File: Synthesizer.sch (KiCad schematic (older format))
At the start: 39 parts, among them J9 MCU_debug, SW1 SW_Push, SW10 SW_Push, SW11 SW_Push, SW12 SW_Push, SW13 SW_Push, SW2 SW_Push, SW3 SW_Push, SW4 SW_Push, SW5 SW_Push, SW6 SW_Push, SW7 SW_Push, SW8 SW_Push, SW9 SW_Push, U1 EFM32GG11B1xx, U7 EFM32GG11B1xx, Y1 48Mhz

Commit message: Added audio jack and footprint
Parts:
- added J2: AudioJack3, Connector_Audio:Jack_3.5mm_CUI_SJ-3524-SMT_Horizontal, symbol Connector:AudioJack3
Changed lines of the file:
@@
 	5350 15650 5350 15350
 Connection ~ 5350 15350
-	14050 4200 14050 4900
 Wire Wire Line
 	10250 5300 10700 5300
@@
 Wire Wire Line
 	8500 9050 9150 9050
+$Comp
+L Connector:AudioJack3 J2
+U 1 1 5D83EB38
+P 2500 10100
+F 0 "J2" H 2482 10425 50  0000 C CNN
+F 1 "AudioJack3" H 2482 10334 50  0000 C CNN
+F 2 "Connector_Audio:Jack_3.5mm_CUI_SJ-3524-SMT_Horizontal" H 2500 10100 50  0001 C CNN
+F 3 "~" H 2500 10100 50  0001 C CNN
+	1    2500 10100
+	1    0    0    -1
+$EndComp
 $EndSCHEMATC

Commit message: Change the project to use the new MCU
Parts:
- removed C1: 1u, Capacitor_SMD:C_0805_2012Metric_Pad1.15x1.40mm_HandSolder, symbol Device:C
- removed C2, C3, C5, C6, C7, C8: 100n, Capacitor_SMD:C_0805_2012Metric_Pad1.15x1.40mm_HandSolder, symbol Device:C
- removed C4, C9: 10u, Capacitor_SMD:C_0805_2012Metric_Pad1.15x1.40mm_HandSolder, symbol Device:CP1
- removed J9: MCU_debug, Connector_PinHeader_2.54mm:PinHeader_2x10_P2.54mm_Vertical, symbol Synth:MCU_debug
- removed U1: EFM32GG11B1xx, Package_QFP:HTQFP-64-1EP_10x10mm_P0.5mm_EP8x8mm, symbol Synth:EFM32GG11B1xx
- removed U7: EFM32GG11B1xx, Package_QFP:TQFP-64_10x10mm_P0.5mm, symbol Synth:EFM32GG11B1xx
- removed Y1: 48Mhz, Crystal:Crystal_DS10_D1.0mm_L4.3mm_Vertical, symbol Device:Crystal
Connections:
- wire segments 125 -> 63
- no-connect marks 35 -> 1
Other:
- note removed: "10 times samplerate?"
- note removed: "decouplers for the MCU"

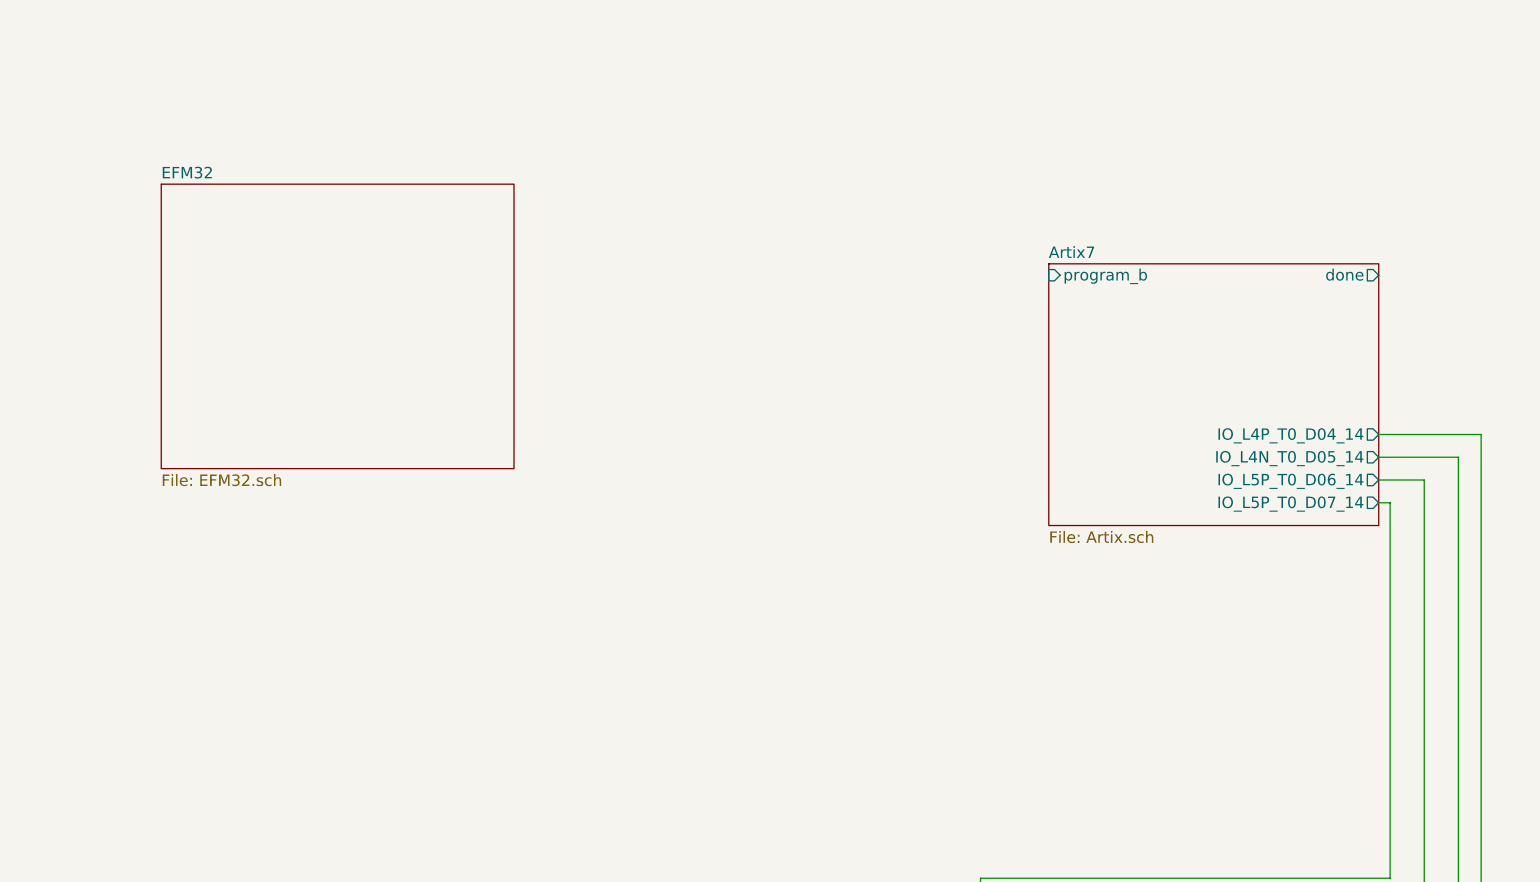
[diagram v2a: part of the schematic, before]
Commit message: Connect the MCU SPI pins to FPGA
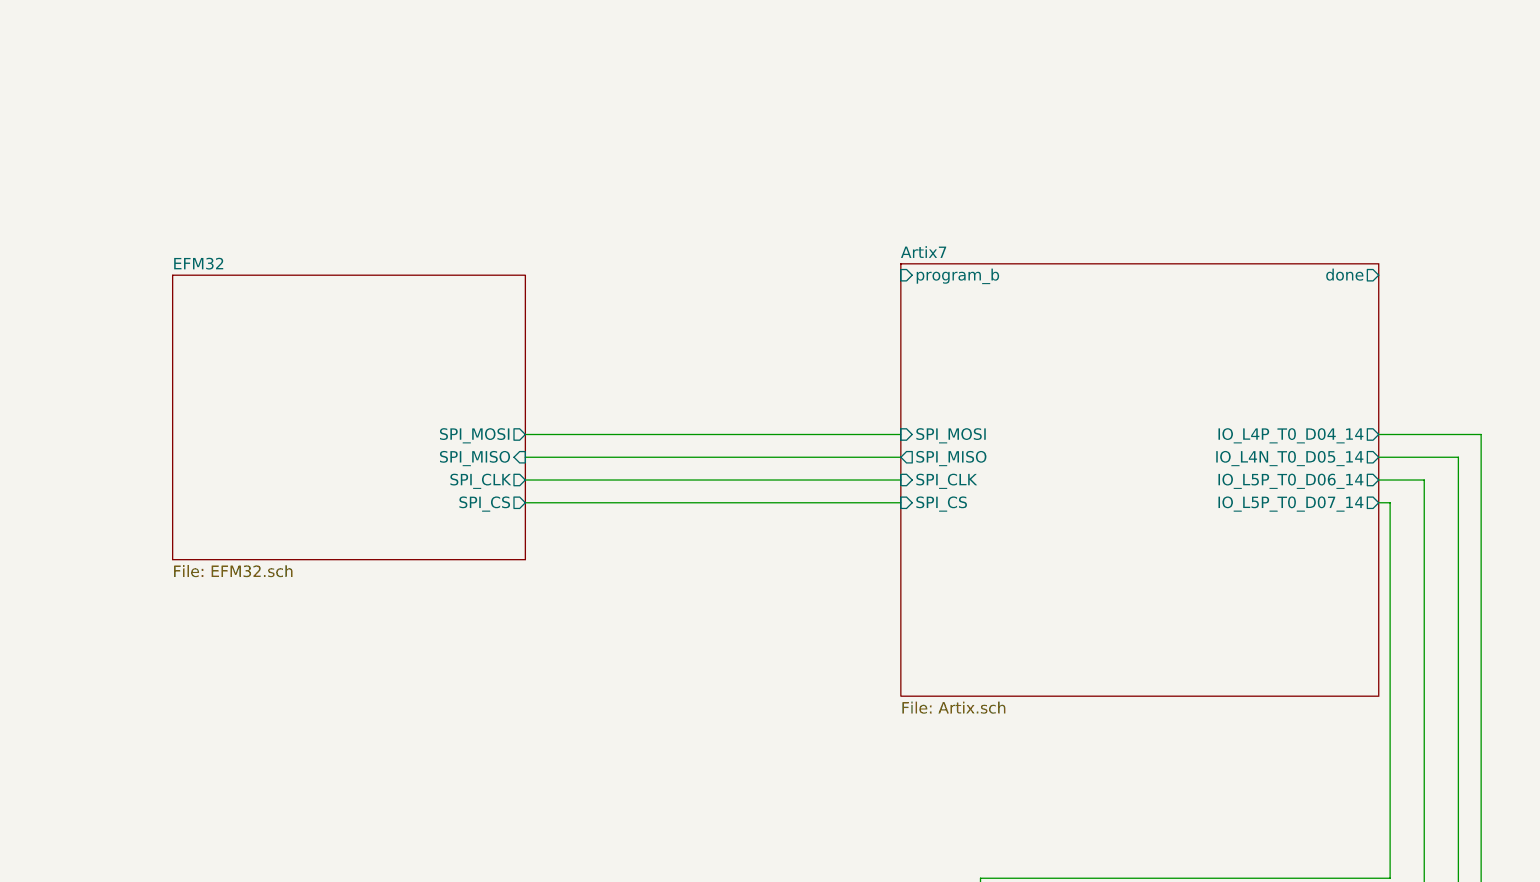
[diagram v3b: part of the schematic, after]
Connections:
- wire segments 63 -> 67
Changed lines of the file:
@@
 $EndDescr
 $Sheet
-S 8800 4550 1450 1150
+S 8150 4550 2100 1900
 U 5D81B1F5
 F0 "Artix7" 50
 F1 "Artix.sch" 50
-F2 "program_b" I L 8800 4600 50
+F2 "program_b" I L 8150 4600 50
 F3 "IO_L4P_T0_D04_14" O R 10250 5300 50
 F4 "IO_L4N_T0_D05_14" O R 10250 5400 50
@@
 F6 "IO_L5P_T0_D07_14" O R 10250 5600 50
 F7 "done" O R 10250 4600 50
+F8 "SPI_MOSI" I L 8150 5300 50
+F9 "SPI_MISO" O L 8150 5400 50
+F10 "SPI_CLK" I L 8150 5500 50
+F11 "SPI_CS" I L 8150 5600 50
 $EndSheet
 $Sheet
@@
 $EndComp
 $Sheet
-S 4900 4200 1550 1250
+S 4950 4600 1550 1250
 U 5D8502F2
 F0 "EFM32" 50
 F1 "EFM32.sch" 50
+F2 "SPI_MISO" I R 6500 5400 50
+F3 "SPI_CLK" O R 6500 5500 50
+F4 "SPI_CS" O R 6500 5600 50
+F5 "SPI_MOSI" O R 6500 5300 50
 $EndSheet
+Wire Wire Line
+	6500 5300 8150 5300
+Wire Wire Line
+	6500 5400 8150 5400
+Wire Wire Line
+	6500 5500 8150 5500
+Wire Wire Line
+	8150 5600 6500 5600
 $EndSCHEMATC

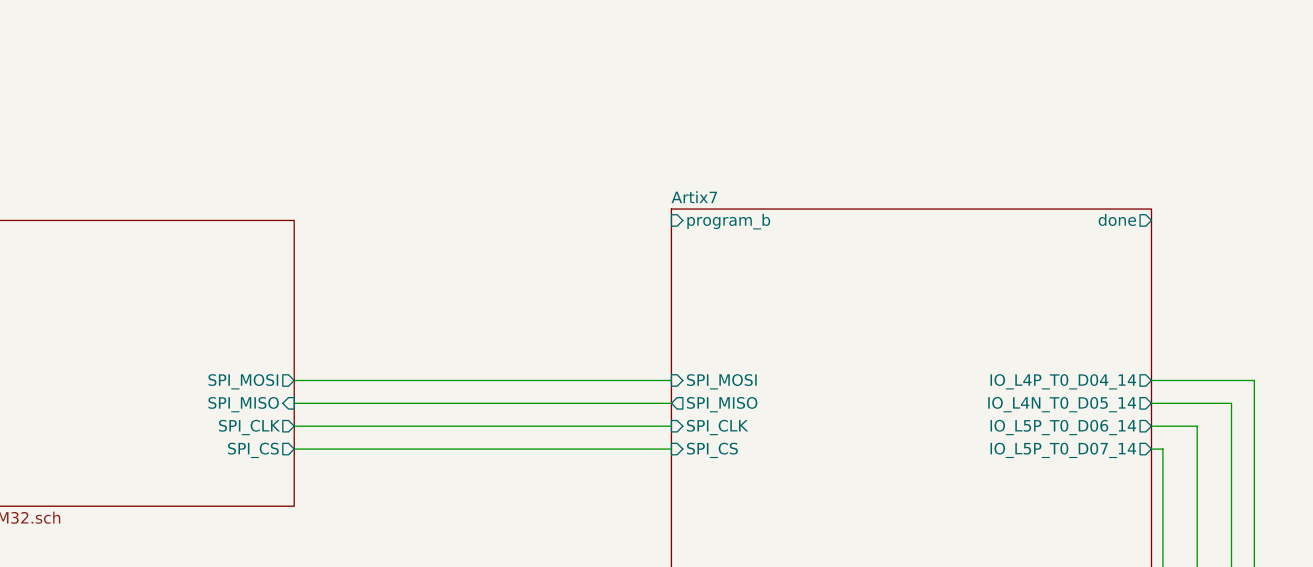
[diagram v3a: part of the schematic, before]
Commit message: Connect FPGA done and program_b pin to some pins on the MCU
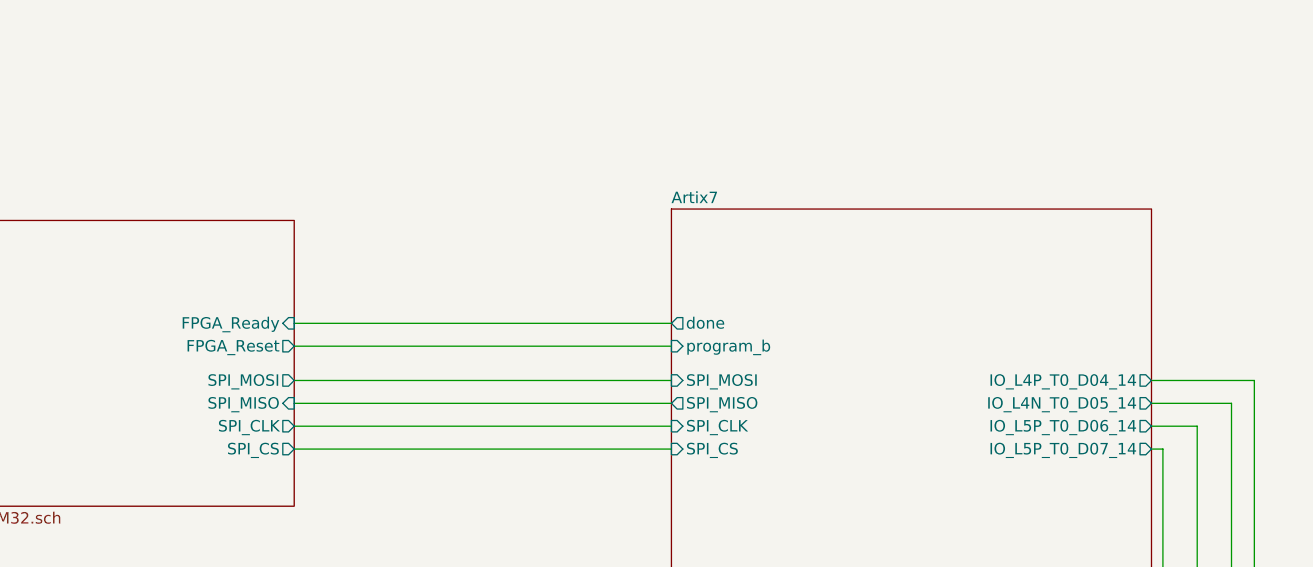
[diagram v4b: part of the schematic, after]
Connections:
- wire segments 67 -> 69
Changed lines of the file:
@@
 EESchema Schematic File Version 4
+LIBS:Synthesizer-cache
 EELAYER 30 0
 EELAYER END
@@
 F0 "Artix7" 50
 F1 "Artix.sch" 50
-F2 "program_b" I L 8150 4600 50
+F2 "program_b" I L 8150 5150 50
 F3 "IO_L4P_T0_D04_14" O R 10250 5300 50
 F4 "IO_L4N_T0_D05_14" O R 10250 5400 50
 F5 "IO_L5P_T0_D06_14" O R 10250 5500 50
 F6 "IO_L5P_T0_D07_14" O R 10250 5600 50
-F7 "done" O R 10250 4600 50
+F7 "done" O L 8150 5050 50
 F8 "SPI_MOSI" I L 8150 5300 50
 F9 "SPI_MISO" O L 8150 5400 50
@@
 F4 "SPI_CS" O R 6500 5600 50
 F5 "SPI_MOSI" O R 6500 5300 50
+F6 "FPGA_Ready" I R 6500 5050 50
+F7 "FPGA_Reset" O R 6500 5150 50
 $EndSheet
 Wire Wire Line
@@
 Wire Wire Line
 	8150 5600 6500 5600
+Wire Wire Line
+	6500 5150 8150 5150
+Wire Wire Line
+	8150 5050 6500 5050
 $EndSCHEMATC

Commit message: Add USB symbol and pins
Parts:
- added J?: USB_B, symbol Connector:USB_B
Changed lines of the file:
@@
 Wire Wire Line
 	8150 5050 6500 5050
+$Comp
+L Connector:USB_B J?
+U 1 1 5D8E7346
+P 1600 5100
+F 0 "J?" H 1657 5567 50  0000 C CNN
+F 1 "USB_B" H 1657 5476 50  0000 C CNN
+F 2 "" H 1750 5050 50  0001 C CNN
+F 3 " ~" H 1750 5050 50  0001 C CNN
+	1    1600 5100
+	1    0    0    -1
+$EndComp
 $EndSCHEMATC

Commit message: Wired up minijack and micro-USB.
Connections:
- wire segments 69 -> 74
- no-connect marks 1 -> 4
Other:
- note added: "I think this makes sense?"
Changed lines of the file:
@@
 EESchema Schematic File Version 4
-LIBS:Synthesizer-cache
 EELAYER 30 0
 EELAYER END
@@
 $EndSheet
 $Sheet
-S 13750 7050 2150 1400
+S 15050 4300 2150 1400
 U 5DC1AA2E
 F0 "PSU" 50
 F1 "PSU.sch" 50
-F2 "POWER_IN" I L 13750 7200 50
-F3 "3.3V" I R 15900 7350 50
-F4 "3.3VA" I R 15900 7450 50
-F5 "1.8V" I R 15900 7250 50
-F6 "1.0V" I R 15900 7150 50
+F2 "POWER_IN" I L 15050 4450 50
+F3 "3.3V" I R 17200 4600 50
+F4 "3.3VA" I R 17200 4700 50
+F5 "1.8V" I R 17200 4500 50
+F6 "1.0V" I R 17200 4400 50
 $EndSheet
-$Comp
-L power:VCC #PWR0101
-U 1 1 5DF2B372
-P 13450 7200
-F 0 "#PWR0101" H 13450 7050 50  0001 C CNN
-F 1 "VCC" V 13468 7327 50  0000 L CNN
-F 2 "" H 13450 7200 50  0001 C CNN
-F 3 "" H 13450 7200 50  0001 C CNN
-	1    13450 7200
-	0    -1   -1   0
-$EndComp
-Wire Wire Line
-	13450 7200 13750 7200
-Wire Wire Line
-	15900 7250 16100 7250
-Wire Wire Line
-	16100 7350 15900 7350
-Wire Wire Line
-	15900 7450 16100 7450
+Wire Wire Line
+	17200 4500 17400 4500
+Wire Wire Line
+	17400 4600 17200 4600
+Wire Wire Line
+	17200 4700 17400 4700
 Wire Wire Line
 	5300 2200 5300 2400
@@
 L power:+1V8 #PWR0106
 U 1 1 5E05CCC0
-P 16100 7250
-F 0 "#PWR0106" H 16100 7100 50  0001 C CNN
-F 1 "+1V8" V 16115 7378 50  0000 L CNN
-F 2 "" H 16100 7250 50  0001 C CNN
-F 3 "" H 16100 7250 50  0001 C CNN
-	1    16100 7250
+P 17400 4500
+F 0 "#PWR0106" H 17400 4350 50  0001 C CNN
+F 1 "+1V8" V 17415 4628 50  0000 L CNN
+F 2 "" H 17400 4500 50  0001 C CNN
+F 3 "" H 17400 4500 50  0001 C CNN
+	1    17400 4500
 	0    1    1    0
 $EndComp
@@
 L power:+3.3V #PWR0107
 U 1 1 5E05D9B9
-P 16100 7350
-F 0 "#PWR0107" H 16100 7200 50  0001 C CNN
-F 1 "+3.3V" V 16115 7478 50  0000 L CNN
-F 2 "" H 16100 7350 50  0001 C CNN
-F 3 "" H 16100 7350 50  0001 C CNN
-	1    16100 7350
+P 17400 4600
+F 0 "#PWR0107" H 17400 4450 50  0001 C CNN
+F 1 "+3.3V" V 17415 4728 50  0000 L CNN
+F 2 "" H 17400 4600 50  0001 C CNN
+F 3 "" H 17400 4600 50  0001 C CNN
+	1    17400 4600
 	0    1    1    0
 $EndComp
@@
 L power:+3.3VA #PWR0108
 U 1 1 5E05DF67
-P 16100 7450
-F 0 "#PWR0108" H 16100 7300 50  0001 C CNN
-F 1 "+3.3VA" V 16115 7578 50  0000 L CNN
-F 2 "" H 16100 7450 50  0001 C CNN
-F 3 "" H 16100 7450 50  0001 C CNN
-	1    16100 7450
+P 17400 4700
+F 0 "#PWR0108" H 17400 4550 50  0001 C CNN
+F 1 "+3.3VA" V 17415 4828 50  0000 L CNN
+F 2 "" H 17400 4700 50  0001 C CNN
+F 3 "" H 17400 4700 50  0001 C CNN
+	1    17400 4700
 	0    1    1    0
 $EndComp
@@
 	4900 2200 4900 2400
 Wire Wire Line
-	16100 7150 15900 7150
+	17400 4400 17200 4400
 $Comp
 L power:+1V0 #PWR0105
 U 1 1 5E05BC61
-P 16100 7150
-F 0 "#PWR0105" H 16100 7000 50  0001 C CNN
-F 1 "+1V0" V 16115 7278 50  0000 L CNN
-F 2 "" H 16100 7150 50  0001 C CNN
-F 3 "" H 16100 7150 50  0001 C CNN
-	1    16100 7150
+P 17400 4400
+F 0 "#PWR0105" H 17400 4250 50  0001 C CNN
+F 1 "+1V0" V 17415 4528 50  0000 L CNN
+F 2 "" H 17400 4400 50  0001 C CNN
+F 3 "" H 17400 4400 50  0001 C CNN
+	1    17400 4400
 	0    1    1    0
 $EndComp
@@
 L Connector:AudioJack3 J2
 U 1 1 5D83EB38
-P 2500 10100
-F 0 "J2" H 2482 10425 50  0000 C CNN
-F 1 "AudioJack3" H 2482 10334 50  0000 C CNN
-F 2 "Connector_Audio:Jack_3.5mm_CUI_SJ-3524-SMT_Horizontal" H 2500 10100 50  0001 C CNN
-F 3 "~" H 2500 10100 50  0001 C CNN
-	1    2500 10100
-	1    0    0    -1
+P 12200 8200
+F 0 "J2" H 12182 8525 50  0000 C CNN
+F 1 "AudioJack3" H 12182 8434 50  0000 C CNN
+F 2 "Connector_Audio:Jack_3.5mm_CUI_SJ-3524-SMT_Horizontal" H 12200 8200 50  0001 C CNN
+F 3 "~" H 12200 8200 50  0001 C CNN
+	1    12200 8200
+	-1   0    0    1
 $EndComp
 $Sheet
@@
 L Connector:USB_B J?
 U 1 1 5D8E7346
-P 1600 5100
-F 0 "J?" H 1657 5567 50  0000 C CNN
-F 1 "USB_B" H 1657 5476 50  0000 C CNN
-F 2 "" H 1750 5050 50  0001 C CNN
-F 3 " ~" H 1750 5050 50  0001 C CNN
-	1    1600 5100
-	1    0    0    -1
-$EndComp
+P 14350 4650
+F 0 "J?" H 14407 5117 50  0000 C CNN
+F 1 "USB_B" H 14407 5026 50  0000 C CNN
+F 2 "" H 14500 4600 50  0001 C CNN
+F 3 " ~" H 14500 4600 50  0001 C CNN
+	1    14350 4650
+	1    0    0    -1
+$EndComp
+Wire Wire Line
+	11750 8200 12000 8200
+Wire Wire Line
+	11750 8100 12000 8100
+$Comp
+L power:GND #PWR?
+U 1 1 5D88FD38
+P 11900 8400
+F 0 "#PWR?" H 11900 8150 50  0001 C CNN
+F 1 "GND" H 11905 8227 50  0000 C CNN
+F 2 "" H 11900 8400 50  0001 C CNN
+F 3 "" H 11900 8400 50  0001 C CNN
+	1    11900 8400
+	1    0    0    -1
+$EndComp
+Wire Wire Line
+	12000 8300 11900 8300
+Wire Wire Line
+	11900 8300 11900 8400
+$Comp
+L power:GND #PWR?
+U 1 1 5D894417
+P 14350 5200
+F 0 "#PWR?" H 14350 4950 50  0001 C CNN
+F 1 "GND" H 14355 5027 50  0000 C CNN
+F 2 "" H 14350 5200 50  0001 C CNN
+F 3 "" H 14350 5200 50  0001 C CNN
+	1    14350 5200
+	1    0    0    -1
+$EndComp
+Wire Wire Line
+	14350 5050 14350 5200
+Wire Wire Line
+	14650 4450 15050 4450
+NoConn ~ 14650 4650
+NoConn ~ 14650 4750
+NoConn ~ 14250 5050
+Text Notes 14000 4100 0    50   ~ 0
+I think this makes sense?
 $EndSCHEMATC

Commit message: Wired USB-A. Added a capacitor to USB_VBUS in the schematic. No idea what to do about VBUSEN though.
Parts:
- added J?: USB_A, symbol Connector:USB_A
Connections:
- net labels added: +5V
- wire segments 74 -> 80
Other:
- note added: "idk how to connect this"
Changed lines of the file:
@@
 F6 "FPGA_Ready" I R 6500 5050 50
 F7 "FPGA_Reset" O R 6500 5150 50
+F8 "USB_VBUS" I L 4950 4750 50
+F9 "USB_VBUSEN" I L 4950 4850 50
+F10 "USB_D-" U L 4950 5050 50
+F11 "USB_D+" U L 4950 4950 50
 $EndSheet
 Wire Wire Line
@@
 	14350 5050 14350 5200
 Wire Wire Line
-	14650 4450 15050 4450
+	14650 4450 14800 4450
 NoConn ~ 14650 4650
 NoConn ~ 14650 4750
@@
 Text Notes 14000 4100 0    50   ~ 0
 I think this makes sense?
+$Comp
+L Connector:USB_A J?
+U 1 1 5D8BD3E6
+P 3950 4950
+F 0 "J?" H 4007 5417 50  0000 C CNN
+F 1 "USB_A" H 4007 5326 50  0000 C CNN
+F 2 "" H 4100 4900 50  0001 C CNN
+F 3 " ~" H 4100 4900 50  0001 C CNN
+	1    3950 4950
+	1    0    0    -1
+$EndComp
+$Comp
+L power:+5V #PWR?
+U 1 1 5D8C2B59
+P 14800 4300
+F 0 "#PWR?" H 14800 4150 50  0001 C CNN
+F 1 "+5V" H 14815 4473 50  0000 C CNN
+F 2 "" H 14800 4300 50  0001 C CNN
+F 3 "" H 14800 4300 50  0001 C CNN
+	1    14800 4300
+	1    0    0    -1
+$EndComp
+Wire Wire Line
+	14800 4300 14800 4450
+Connection ~ 14800 4450
+Wire Wire Line
+	14800 4450 15050 4450
+$Comp
+L power:GND #PWR?
+U 1 1 5D8C6D8D
+P 3950 5550
+F 0 "#PWR?" H 3950 5300 50  0001 C CNN
+F 1 "GND" H 3955 5377 50  0000 C CNN
+F 2 "" H 3950 5550 50  0001 C CNN
+F 3 "" H 3950 5550 50  0001 C CNN
+	1    3950 5550
+	1    0    0    -1
+$EndComp
+Wire Wire Line
+	3950 5350 3950 5550
+Wire Wire Line
+	4250 4750 4950 4750
+Wire Wire Line
+	4250 4950 4950 4950
+Wire Wire Line
+	4950 5050 4250 5050
+Text Notes 5550 4850 0    50   ~ 0
+idk how to connect this
 $EndSCHEMATC
